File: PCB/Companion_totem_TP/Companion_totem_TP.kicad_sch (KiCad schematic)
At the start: 98 parts, among them J1 Conn_01x02_Socket, J2 Conn_01x02_Socket, J3 Trackpoint module, U1 xiao-ble, U2 xiao-ble

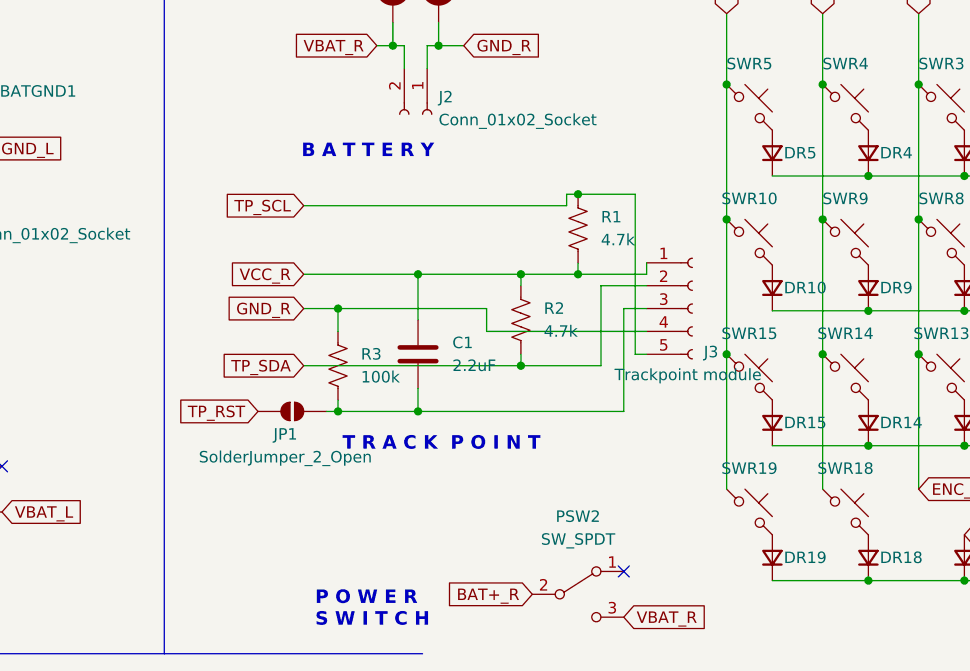
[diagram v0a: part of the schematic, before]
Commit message: Added TP, Split L&R
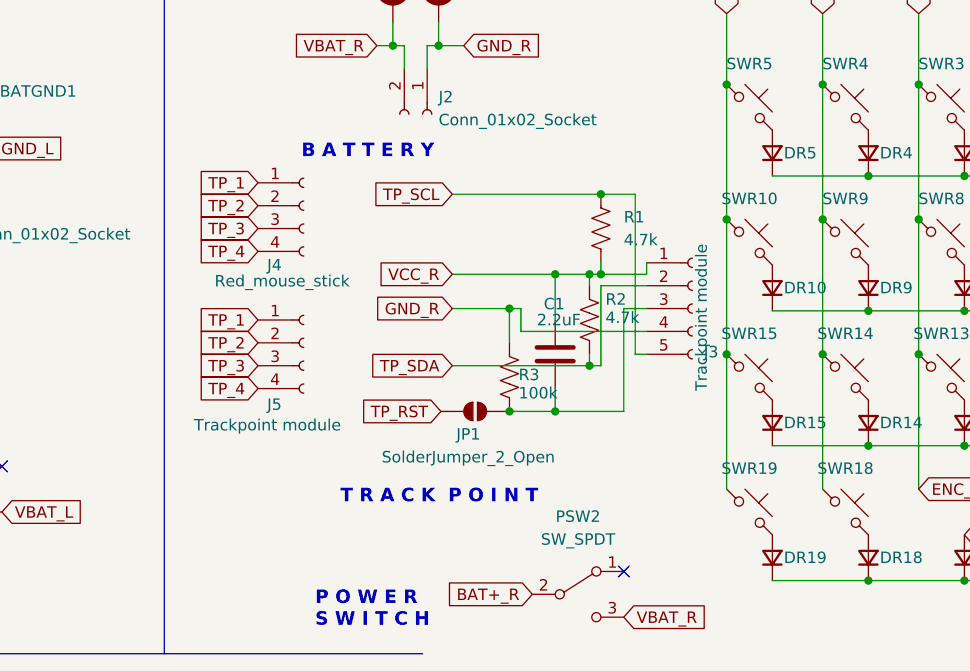
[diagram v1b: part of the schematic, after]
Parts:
- added J4: Red_mouse_stick, TOTEMlib:T460S_TP, symbol Connector:Conn_01x04_Socket
- added J5: Trackpoint module, TOTEMlib:TP_input, symbol Connector:Conn_01x04_Socket
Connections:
- new net TP_1: J4.1 (Pin_1), J5.1 (Pin_1)
- new net TP_2: J4.2 (Pin_2), J5.2 (Pin_2)
- new net TP_3: J4.3 (Pin_3), J5.3 (Pin_3)
- new net TP_4: J4.4 (Pin_4), J5.4 (Pin_4)
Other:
- moved on the sheet: C1, JP1, R1, R2, R3
